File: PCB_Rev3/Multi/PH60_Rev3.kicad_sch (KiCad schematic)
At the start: 46 parts, among them J1 USB_C_Receptacle_USB2.0_16P, J2 Conn_01x02_Pin, J3 Conn_01x04_Socket, J4 Conn_01x02_Pin, U1 nRF52840, U4 LGS5500EP, X2 32.768kHz, X3 Crystal_Generic

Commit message: muliti layout
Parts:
- removed C21: 10u, Capacitor_SMD:C_0402_1005Metric, symbol Device:C
- removed C21: 20u, Capacitor_SMD:C_0402_1005Metric, symbol Device:C
- removed L5: 2.2uH, Inductor_SMD:L_Changjiang_FNR252012S, symbol Device:L
- added C11: 20u, Capacitor_SMD:C_0402_1005Metric, symbol Device:C
- added C9: 10u, Capacitor_SMD:C_0402_1005Metric, symbol Device:C
- added D68: PTVS5V0P1UP, PCM_Diode_SMD_AKL:D_SOD-882_DFN1006-2, symbol PCM_Diode_TVS_AKL:PTVS5V0P1UP
- added L2: 2.2uH, Inductor_SMD:L_Changjiang_FNR252012S, symbol Device:L
- added R12, R13: 10k, PCM_Resistor_SMD_AKL:R_0402_1005Metric, symbol Device:R
- added SW1: SW_SPDT_321, Button_Switch_SMD:SW_SPDT_PCM12, symbol Switch:SW_SPDT_321
- added TH1: 10k_NTC, PCM_4ms_Resistor:R_0603, symbol Device:Thermistor_NTC
- J4: renamed from J3; footprint (none) -> Connector_FFC-FPC:Molex_200528-0040_1x04-1MP_P1.00mm_Horizontal
- renumbered C12 to C1, C20 to C10, C8 to C12, C11 to C13, C9 to C14, C10 to C15, C2 to C16, C4 to C17, C1 to C18, C3 to C19, C14 to C2, C5 to C20, C6 to C21, C7 to C22, C16 to C3, C13 to C4, C15 to C5, C17 to C6, C18 to C7, C19 to C8, D65 to D1, J4 to J1, J1 to J3, L4 to L1, L1 to L4, L2 to L5, R1 to R4, R3 to R5, R4 to R6, R6 to R7, R7 to R8, U1 to U2, X2 to X1, X3 to X2
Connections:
- net +BATT: now also C11.1, L2.2
- net CHRG: now also R15.1; no longer R15.2
- net GND: now also R10.2, C11.2, C9.2; no longer R10.1
- net VBUS: now also D68.1 (K), SW1.1 (C); no longer U4.5 (VH)
- net VBUS_USB: no longer R10.2, U4.2 (VIN)
- net at U4.4 (LX): now also L2.1
- net at U4.7 (VSET/LED): now also R15.2; no longer R15.1
- net at U4.8 (NTC): now also R13.2, TH1.2
- new net: R12.2, R13.1, TH1.1
- new net: SW1.2 (B), U4.5 (VH)
- new net VBUS_in: C9.1, D68.2 (A), R10.1, R12.1, U4.2 (VIN)
- no-connect marks 27 -> 26
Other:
- moved on the sheet: BT1, R10, R14, R15

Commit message: layout
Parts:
- removed D68: PTVS5V0P1UP, PCM_Diode_SMD_AKL:D_SOD-882_DFN1006-2, symbol PCM_Diode_TVS_AKL:PTVS5V0P1UP
- removed SW1: SW_SPDT_321, Button_Switch_SMD:SW_SPDT_PCM12, symbol Switch:SW_SPDT_321
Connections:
- net VBUS_in is gone; now on net VBUS_USB: C9.1, R10.1, R12.1, U4.2 (VIN)

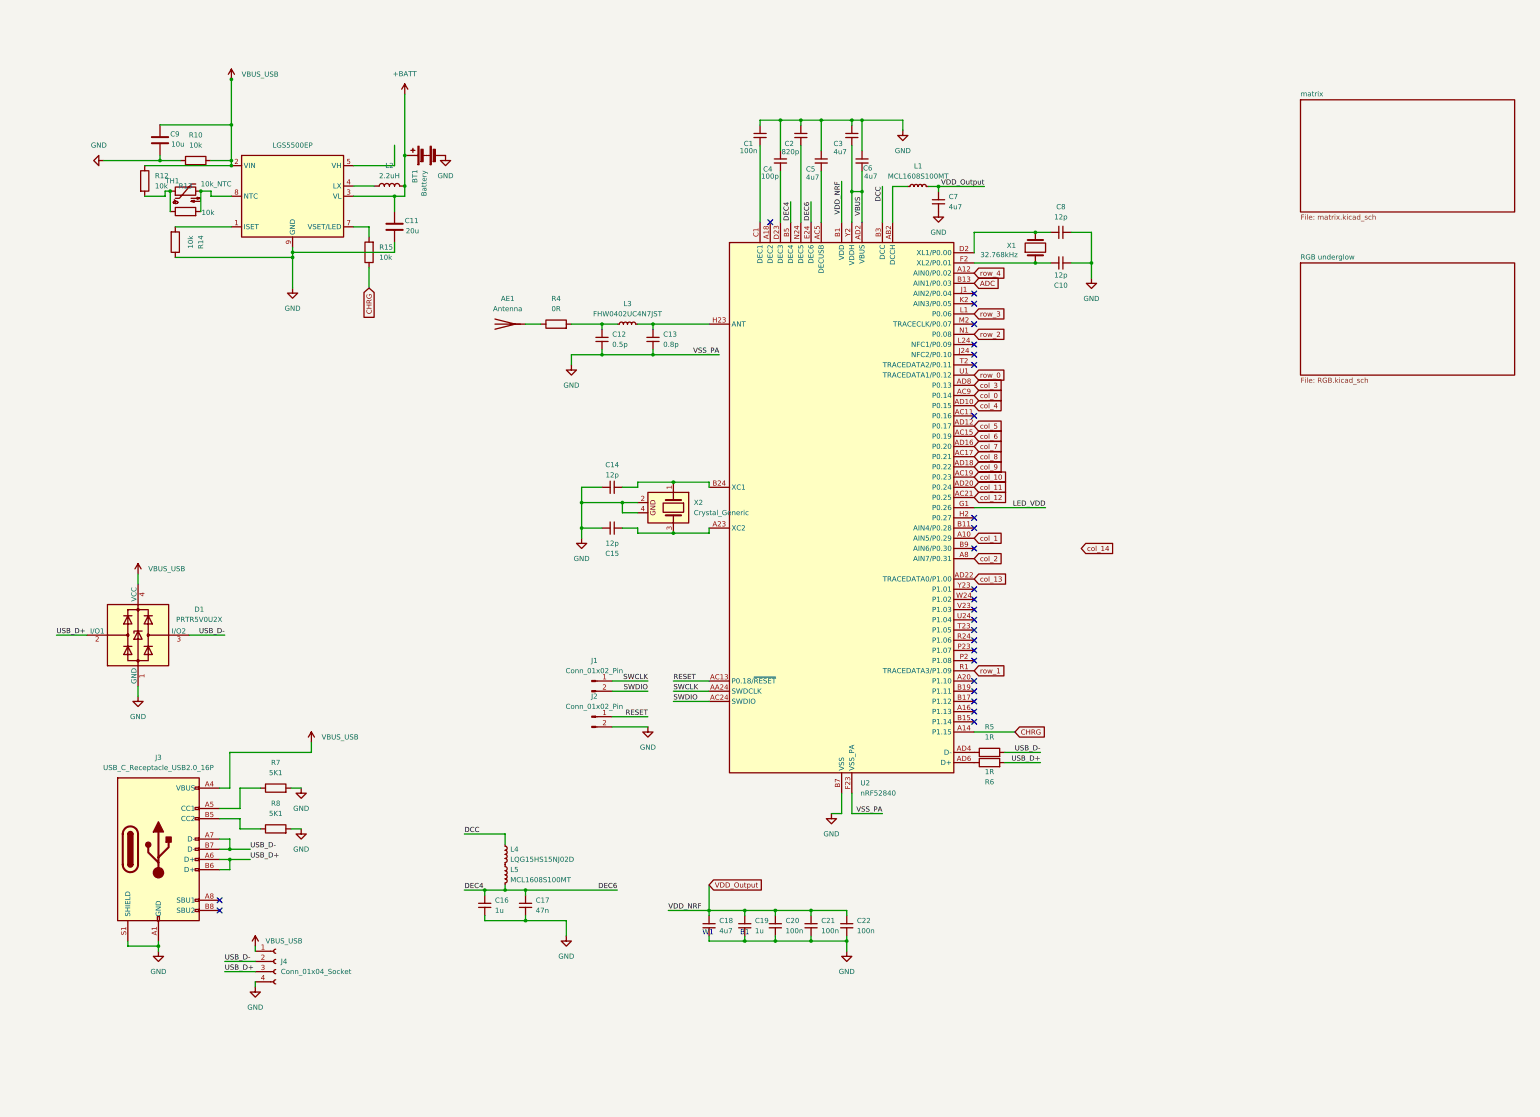
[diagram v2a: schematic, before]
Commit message: With the basic layout and wiring completed, a simple DRC (Digital Router Control) process is performed.
There is an issue with the satellite axis position that needs to be addressed, and there is also an issue with some pad overlap that needs to be resolved.
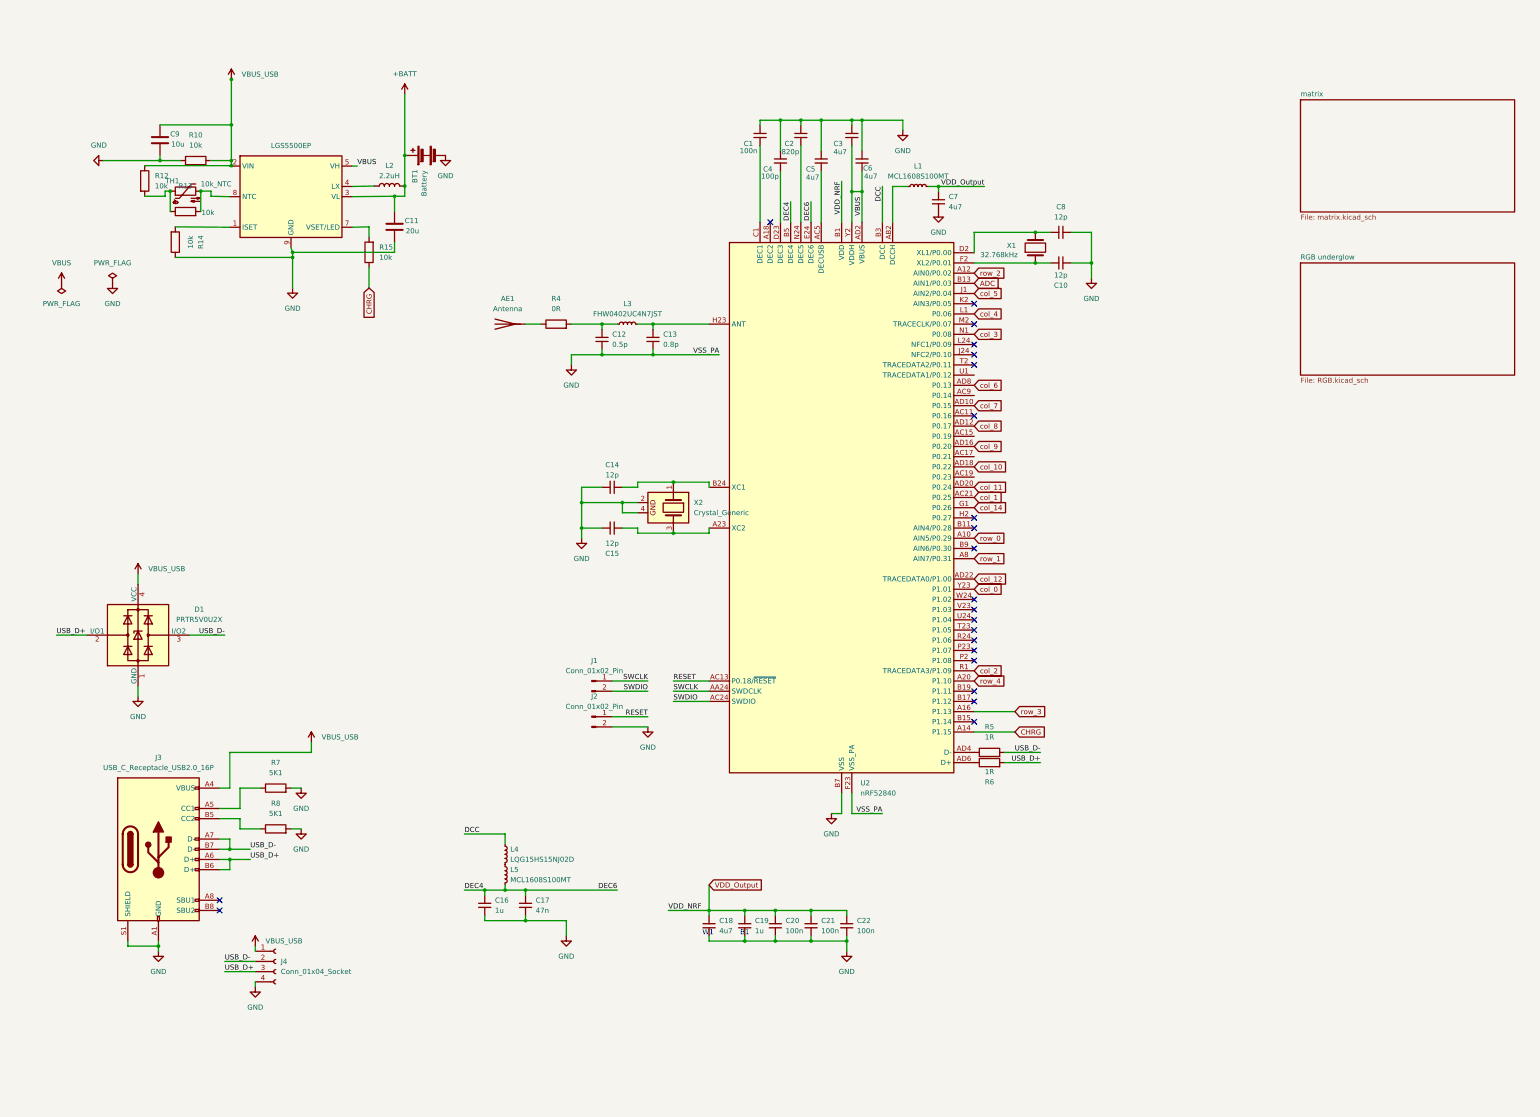
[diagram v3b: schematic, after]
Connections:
- net LED_VDD is gone; now on net col_14: U2.G1 (P0.26)
- net col_13 is gone; now on net col_12: U2.AD22 (TRACEDATA0/P1.00)
- net VBUS: now also U4.5 (VH)
- net col_0: now also U2.Y23 (P1.01); no longer U2.AC9 (P0.14)
- net col_1: now also U2.AC21 (P0.25); no longer U2.A10 (AIN5/P0.29)
- net col_10: now also U2.AD18 (P0.22); no longer U2.AC19 (P0.23)
- net col_12: no longer U2.AC21 (P0.25)
- net col_2: now also U2.R1 (TRACEDATA3/P1.09); no longer U2.A8 (AIN7/P0.31)
- net col_3: now also U2.N1 (P0.08); no longer U2.AD8 (P0.13)
- net col_4: now also U2.L1 (P0.06); no longer U2.AD10 (P0.15)
- net col_5: now also U2.J1 (AIN2/P0.04); no longer U2.AD12 (P0.17)
- net col_6: now also U2.AD8 (P0.13); no longer U2.AC15 (P0.19)
- net col_7: now also U2.AD10 (P0.15); no longer U2.AD16 (P0.20)
- net col_8: now also U2.AD12 (P0.17); no longer U2.AC17 (P0.21)
- net col_9: now also U2.AD16 (P0.20); no longer U2.AD18 (P0.22)
- net row_0: now also U2.A10 (AIN5/P0.29); no longer U2.U1 (TRACEDATA1/P0.12)
- net row_1: now also U2.A8 (AIN7/P0.31); no longer U2.R1 (TRACEDATA3/P1.09)
- net row_2: now also U2.A12 (AIN0/P0.02); no longer U2.N1 (P0.08)
- net row_3: now also U2.A16 (P1.13); no longer U2.L1 (P0.06)
- net row_4: now also U2.A20 (P1.10); no longer U2.A12 (AIN0/P0.02)
- no-connect marks 26 -> 22

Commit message: Delete RGB
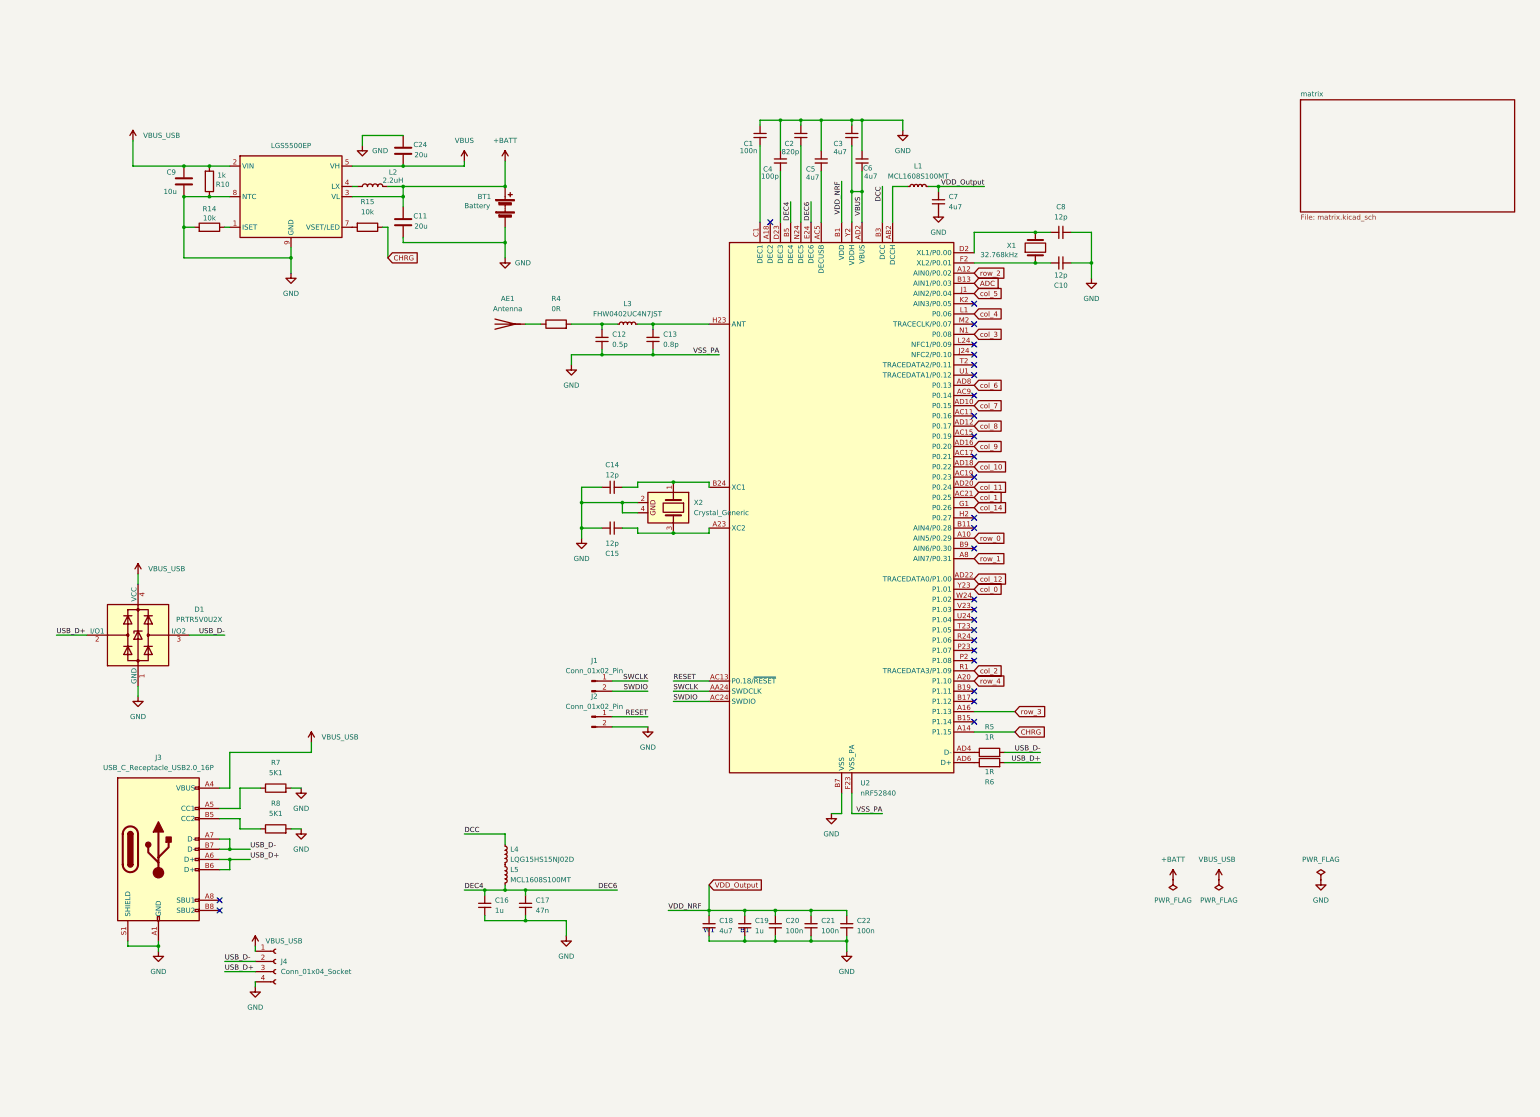
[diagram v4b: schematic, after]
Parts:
- removed R12, R13: 10k, PCM_Resistor_SMD_AKL:R_0402_1005Metric, symbol Device:R
- removed TH1: 10k_NTC, PCM_4ms_Resistor:R_0603, symbol Device:Thermistor_NTC
- added C24: 20u, Capacitor_SMD:C_0402_1005Metric, symbol Device:C
- R10: value 10k -> 1k
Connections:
- net GND: now also R10.1, R14.2, U4.8 (NTC), C24.1; no longer R10.2, R14.1
- net VBUS: now also C24.2
- net VBUS_USB: now also R10.2; no longer R10.1
- net at U4.1 (ISET): now also R14.1; no longer R14.2
- no-connect marks 22 -> 27
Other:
- removed sheet RGB underglow
- moved on the sheet: BT1, C11, C9, L2, R10, R14, R15

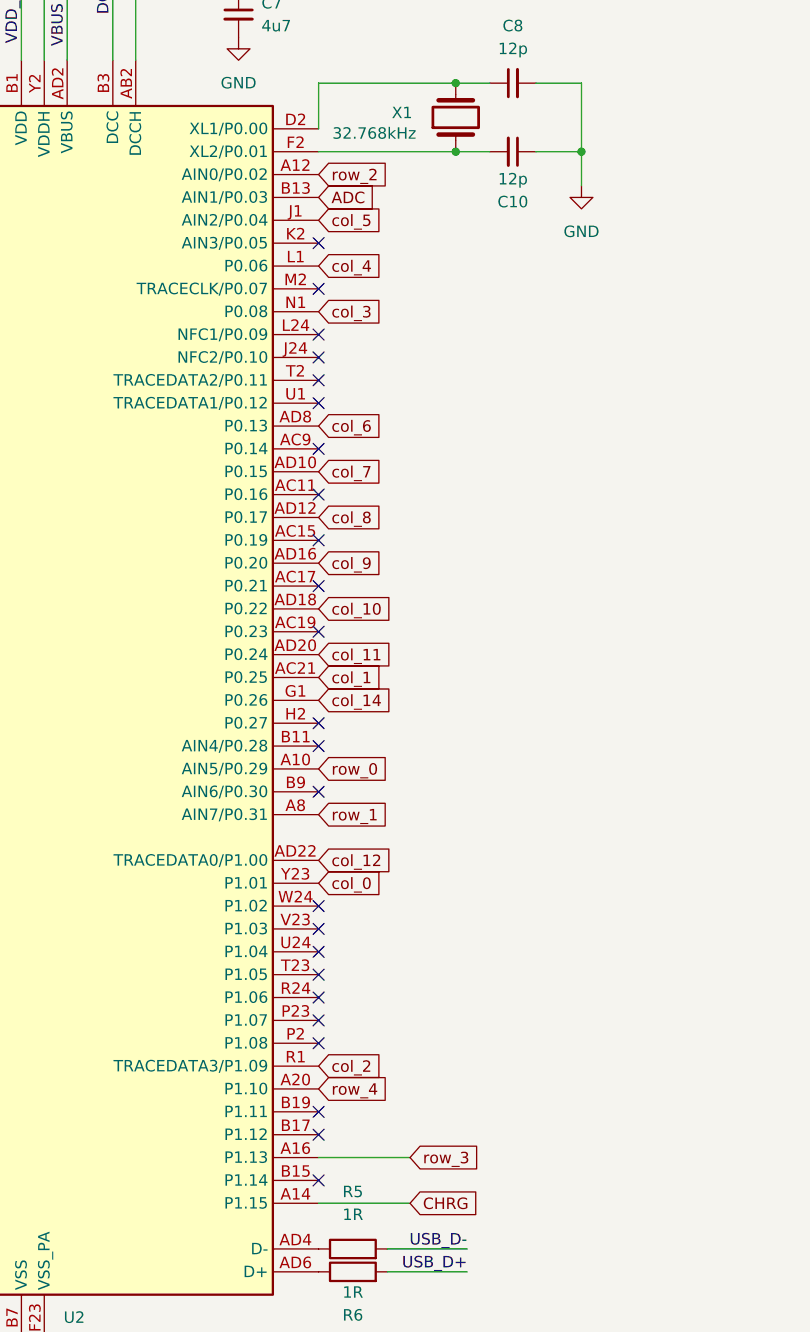
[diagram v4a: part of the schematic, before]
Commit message: drc and pcb layout
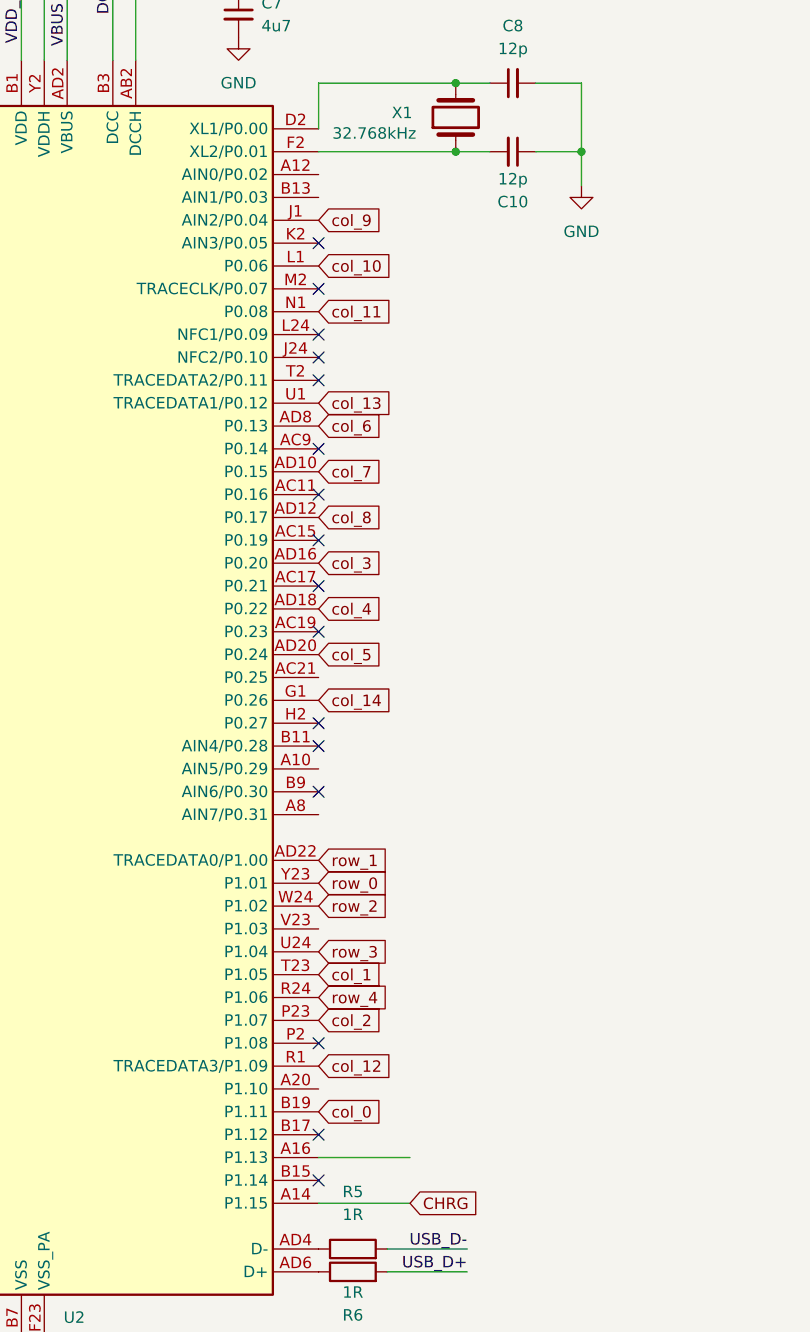
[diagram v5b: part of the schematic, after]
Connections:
- net col_0: now also U2.B19 (P1.11); no longer U2.Y23 (P1.01)
- net col_1: now also U2.T23 (P1.05); no longer U2.AC21 (P0.25)
- net col_10: now also U2.L1 (P0.06); no longer U2.AD18 (P0.22)
- net col_11: now also U2.N1 (P0.08); no longer U2.AD20 (P0.24)
- net col_12: now also U2.R1 (TRACEDATA3/P1.09); no longer U2.AD22 (TRACEDATA0/P1.00)
- net col_2: now also U2.P23 (P1.07); no longer U2.R1 (TRACEDATA3/P1.09)
- net col_3: now also U2.AD16 (P0.20); no longer U2.N1 (P0.08)
- net col_4: now also U2.AD18 (P0.22); no longer U2.L1 (P0.06)
- net col_5: now also U2.AD20 (P0.24); no longer U2.J1 (AIN2/P0.04)
- net col_9: now also U2.J1 (AIN2/P0.04); no longer U2.AD16 (P0.20)
- net row_0: now also U2.Y23 (P1.01); no longer U2.A10 (AIN5/P0.29)
- net row_1: now also U2.AD22 (TRACEDATA0/P1.00); no longer U2.A8 (AIN7/P0.31)
- net row_2: now also U2.W24 (P1.02); no longer U2.A12 (AIN0/P0.02)
- net row_3: now also U2.U24 (P1.04); no longer U2.A16 (P1.13)
- net row_4: now also U2.R24 (P1.06); no longer U2.A20 (P1.10)
- net col_13: now reaches U2.U1 (TRACEDATA1/P0.12)
- net ADC: no longer names the net of U2.B13 (AIN1/P0.03)
- no-connect marks 27 -> 19

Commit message: drc and layout
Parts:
- added R11: 100k, PCM_Resistor_SMD_AKL:R_0402_1005Metric, symbol Device:R
- added R9: 33k, PCM_Resistor_SMD_AKL:R_0402_1005Metric, symbol Device:R
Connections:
- net +BATT: now also R9.2
- net GND: now also R11.2
- net batt_level: now reaches U2.B13 (AIN1/P0.03)
- net batt_level: now also R11.1, R9.1

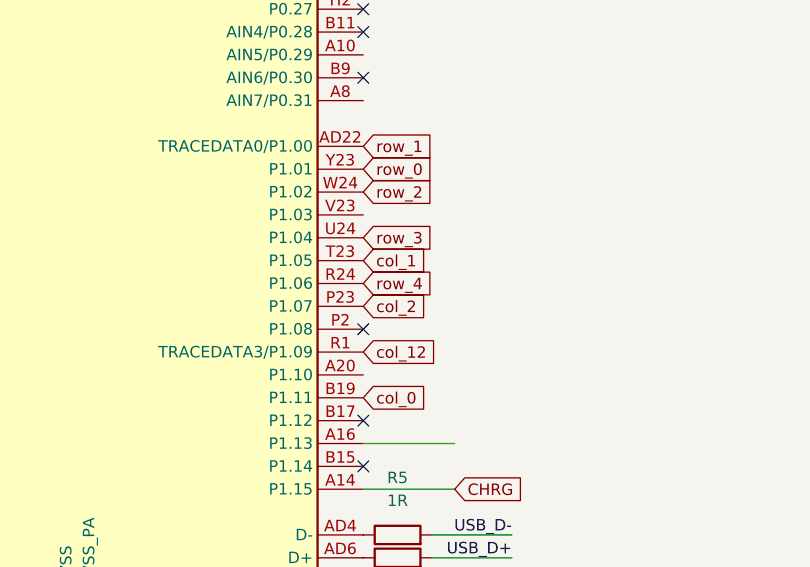
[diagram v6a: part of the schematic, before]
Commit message: layout and drc
简单完成基础布局及走线，drc‘完成，未经审核
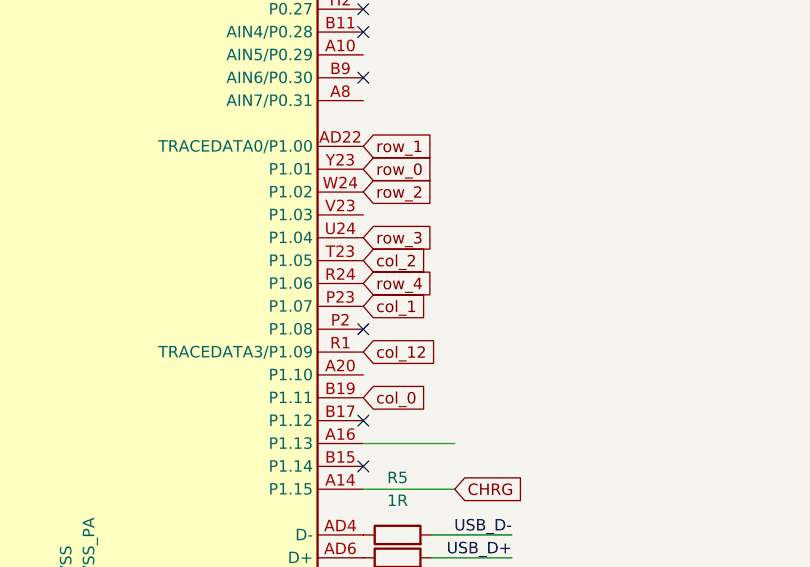
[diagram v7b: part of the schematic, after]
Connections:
- net col_1: now also U2.P23 (P1.07); no longer U2.T23 (P1.05)
- net col_2: now also U2.T23 (P1.05); no longer U2.P23 (P1.07)
